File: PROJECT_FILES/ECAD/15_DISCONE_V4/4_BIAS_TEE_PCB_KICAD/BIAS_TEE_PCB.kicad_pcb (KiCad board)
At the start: 2 copper layers, 43 x 24 mm, 24 parts

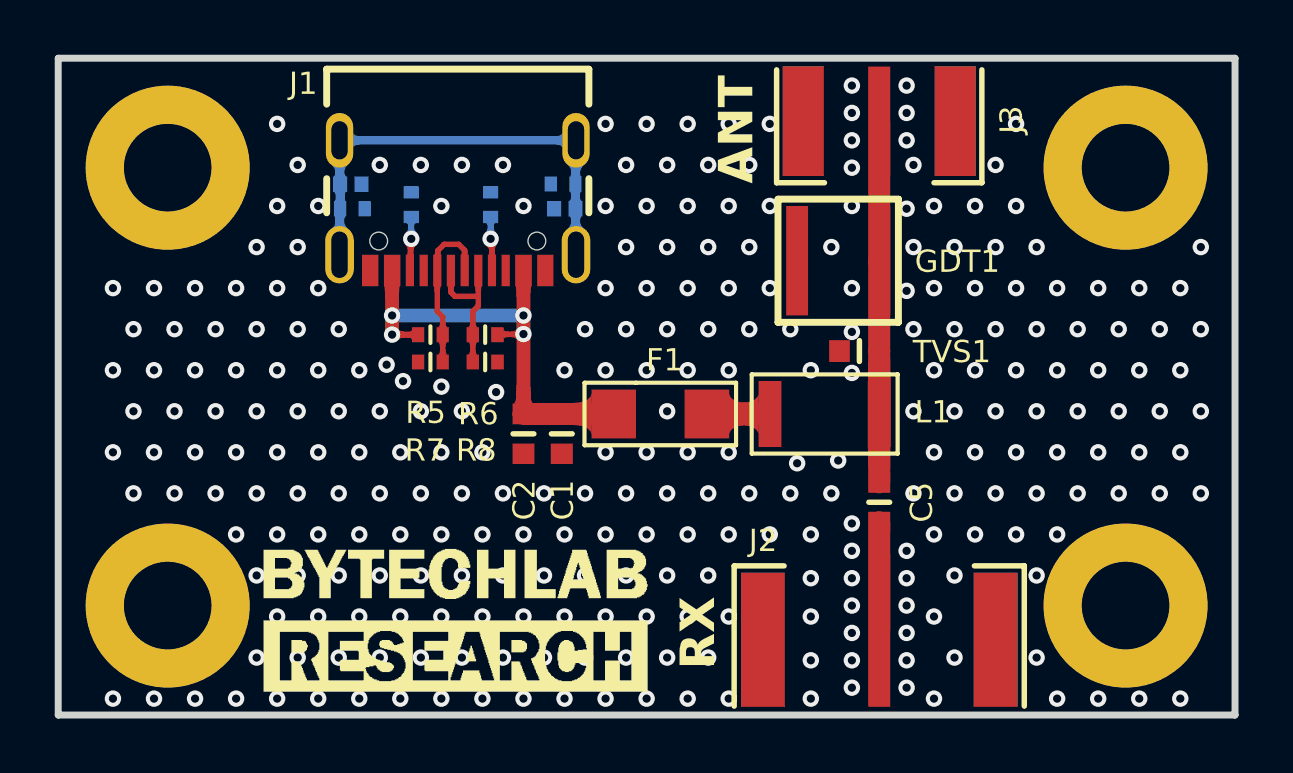
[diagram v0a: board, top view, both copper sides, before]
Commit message: Update jobset & exported files
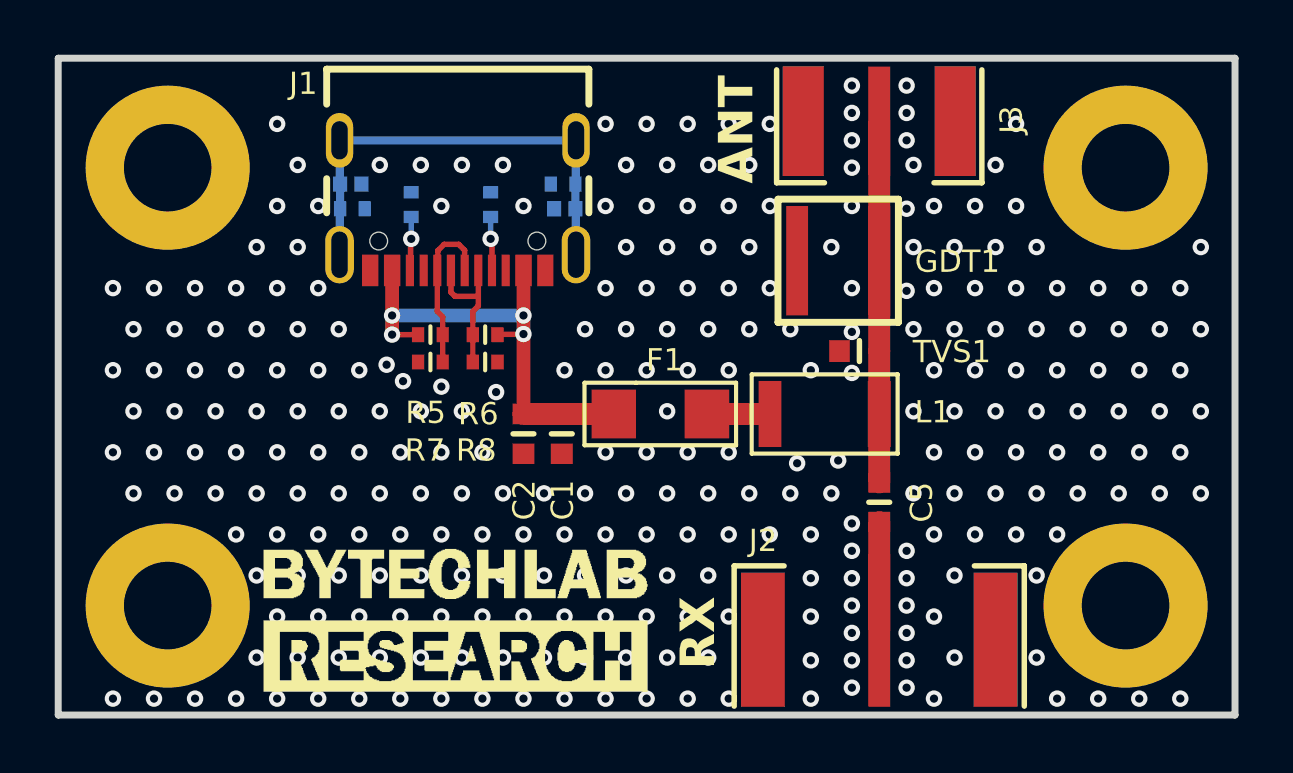
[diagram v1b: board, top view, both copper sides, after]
